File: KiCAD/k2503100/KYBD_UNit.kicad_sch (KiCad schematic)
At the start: 88 parts, among them Q301 2N3904, Q302 2N3904, Q303 2N3904, Q304 2N3904, Q305 2N3904, Q306 2N3904, Q307 2N3904, Q308 2N3904, Q309 2N3904, Q310 2N3904, Q311 2N3904, Q312 2N3904

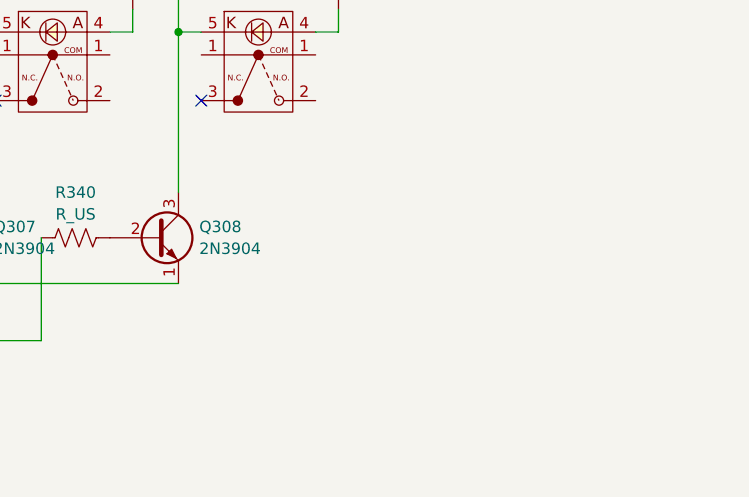
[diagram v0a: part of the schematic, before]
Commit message: 未使用回路の削除
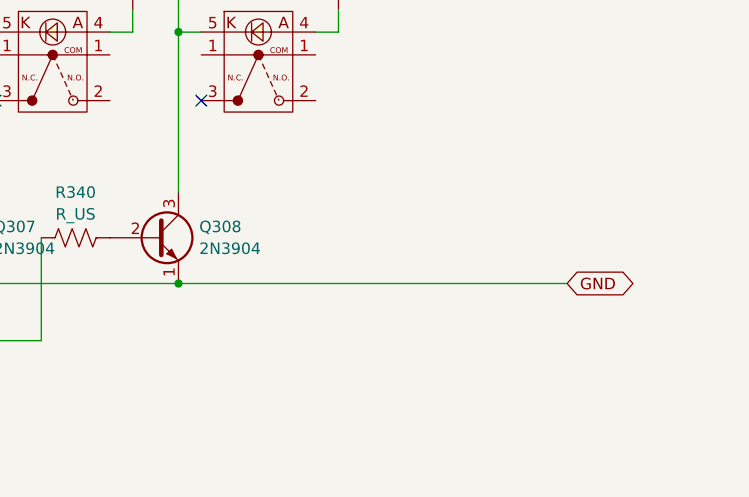
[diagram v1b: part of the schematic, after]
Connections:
- net GND: now reaches Q301.1 (E), Q302.1 (E), Q303.1 (E), Q304.1 (E), Q305.1 (E), Q306.1 (E), Q307.1 (E), Q308.1 (E)
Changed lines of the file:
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@@
 	)
 	(junction
+		(at 213.36 154.94)
+		(diameter 0)
+		(color 0 0 0 0)
+	)
+	(junction
 		(at 231.14 90.17)
 		(diameter 0)
@@
 	(wire
 		(pts
+			(xy 213.36 154.94) (xy 256.54 154.94)
+		)
+		(stroke
+			(width 0)
+			(type default)
+		)
+	)
+	(wire
+		(pts
 			(xy 78.74 127) (xy 76.2 127)
 		)
@@
 		)
 	)
+	(global_label "GND"
+		(shape bidirectional)
+		(at 256.54 154.94 0)
+		(fields_autoplaced yes)
+		(effects
+			(font
+				(size 1.27 1.27)
+			)
+			(justify left)
+		)
+		(property "Intersheetrefs" "${INTERSHEET_REFS}"
+			(at 264.5068 154.94 0)
+			(effects
+				(font
+					(size 1.27 1.27)
+				)
+				(justify left)
+				(hide yes)
+			)
+		)
+	)
 	(global_label "5V"
 		(shape input)
@@
 	)
 	(symbol
-		(lib_name "K2503100:MP86A1")
 		(lib_id "K2503100:MP86A1")
 		(at 153.67 43.18 0)
@@
 	)
 	(symbol
-		(lib_name "K2503100:MP86A1")
 		(lib_id "K2503100:MP86A1")
 		(at 130.81 43.18 0)
@@
 	)
 	(symbol
-		(lib_name "K2503100:MP86A1")
 		(lib_id "K2503100:MP86A1")
 		(at 176.53 96.52 0)
@@
 	)
 	(symbol
-		(lib_name "K2503100:MP86A1")
 		(lib_id "K2503100:MP86A1")
 		(at 62.23 69.85 0)
@@
 	)
 	(symbol
-		(lib_name "K2503100:MP86A1")
 		(lib_id "K2503100:MP86A1")
 		(at 62.23 96.52 0)
@@
 	)
 	(symbol
-		(lib_name "K2503100:MP86A1")
 		(lib_id "K2503100:MP86A1")
 		(at 176.53 69.85 0)
@@
 	)
 	(symbol
-		(lib_name "K2503100:MP86A1")
 		(lib_id "K2503100:MP86A1")
 		(at 199.39 43.18 0)
@@
 	)
 	(symbol
-		(lib_name "K2503100:MP86A1")
 		(lib_id "K2503100:MP86A1")
 		(at 62.23 43.18 0)
@@
 	)
 	(symbol
-		(lib_name "K2503100:MP86A1")
 		(lib_id "K2503100:MP86A1")
 		(at 222.25 96.52 0)
@@
 	)
 	(symbol
-		(lib_name "K2503100:MP86A1")
 		(lib_id "K2503100:MP86A1")
 		(at 85.09 96.52 0)
@@
 	)
 	(symbol
-		(lib_name "K2503100:MP86A1")
 		(lib_id "K2503100:MP86A1")
 		(at 199.39 123.19 0)
@@
 	)
 	(symbol
-		(lib_name "K2503100:MP86A1")
 		(lib_id "K2503100:MP86A1")
 		(at 199.39 96.52 0)
@@
 	)
 	(symbol
-		(lib_name "K2503100:MP86A1")
 		(lib_id "K2503100:MP86A1")
 		(at 199.39 69.85 0)
@@
 	)
 	(symbol
-		(lib_name "K2503100:MP86A1")
 		(lib_id "K2503100:MP86A1")
 		(at 107.95 96.52 0)
@@
 	)
 	(symbol
-		(lib_name "K2503100:MP86A1")
 		(lib_id "K2503100:MP86A1")
 		(at 176.53 43.18 0)
@@
 	)
 	(symbol
-		(lib_name "K2503100:MP86A1")
 		(lib_id "K2503100:MP86A1")
 		(at 222.25 123.19 0)
@@
 	)
 	(symbol
-		(lib_name "K2503100:MP86A1")
 		(lib_id "K2503100:MP86A1")
 		(at 85.09 69.85 0)
@@
 	)
 	(symbol
-		(lib_name "K2503100:MP86A1")
 		(lib_id "K2503100:MP86A1")
 		(at 153.67 96.52 0)
@@
 	)
 	(symbol
-		(lib_name "K2503100:MP86A1")
 		(lib_id "K2503100:MP86A1")
 		(at 130.81 123.19 0)
@@
 	)
 	(symbol
-		(lib_name "K2503100:MP86A1")
 		(lib_id "K2503100:MP86A1")
 		(at 153.67 69.85 0)
@@
 	)
 	(symbol
-		(lib_name "K2503100:MP86A1")
 		(lib_id "K2503100:MP86A1")
 		(at 153.67 123.19 0)
@@
 	)
 	(symbol
-		(lib_name "K2503100:MP86A1")
 		(lib_id "K2503100:MP86A1")
 		(at 176.53 123.19 0)
@@
 	)
 	(symbol
-		(lib_name "K2503100:MP86A1")
 		(lib_id "K2503100:MP86A1")
 		(at 130.81 96.52 0)
@@
 	)
 	(symbol
-		(lib_name "K2503100:MP86A1")
 		(lib_id "K2503100:MP86A1")
 		(at 107.95 69.85 0)
@@
 	)
 	(symbol
-		(lib_name "K2503100:MP86A1")
 		(lib_id "K2503100:MP86A1")
 		(at 62.23 123.19 0)
@@
 	)
 	(symbol
-		(lib_name "K2503100:MP86A1")
 		(lib_id "K2503100:MP86A1")
 		(at 222.25 69.85 0)
@@
 	)
 	(symbol
-		(lib_name "K2503100:MP86A1")
 		(lib_id "K2503100:MP86A1")
 		(at 130.81 69.85 0)
@@
 	)
 	(symbol
-		(lib_name "K2503100:MP86A1")
 		(lib_id "K2503100:MP86A1")
 		(at 85.09 43.18 0)
@@
 	)
 	(symbol
-		(lib_name "K2503100:MP86A1")
 		(lib_id "K2503100:MP86A1")
 		(at 107.95 43.18 0)
@@
 	)
 	(symbol
-		(lib_name "K2503100:MP86A1")
 		(lib_id "K2503100:MP86A1")
 		(at 222.25 43.18 0)
@@
 	)
 	(symbol
-		(lib_name "K2503100:MP86A1")
 		(lib_id "K2503100:MP86A1")
 		(at 85.09 123.19 0)
@@
 	)
 	(symbol
-		(lib_name "K2503100:MP86A1")
 		(lib_id "K2503100:MP86A1")
 		(at 107.95 123.19 0)

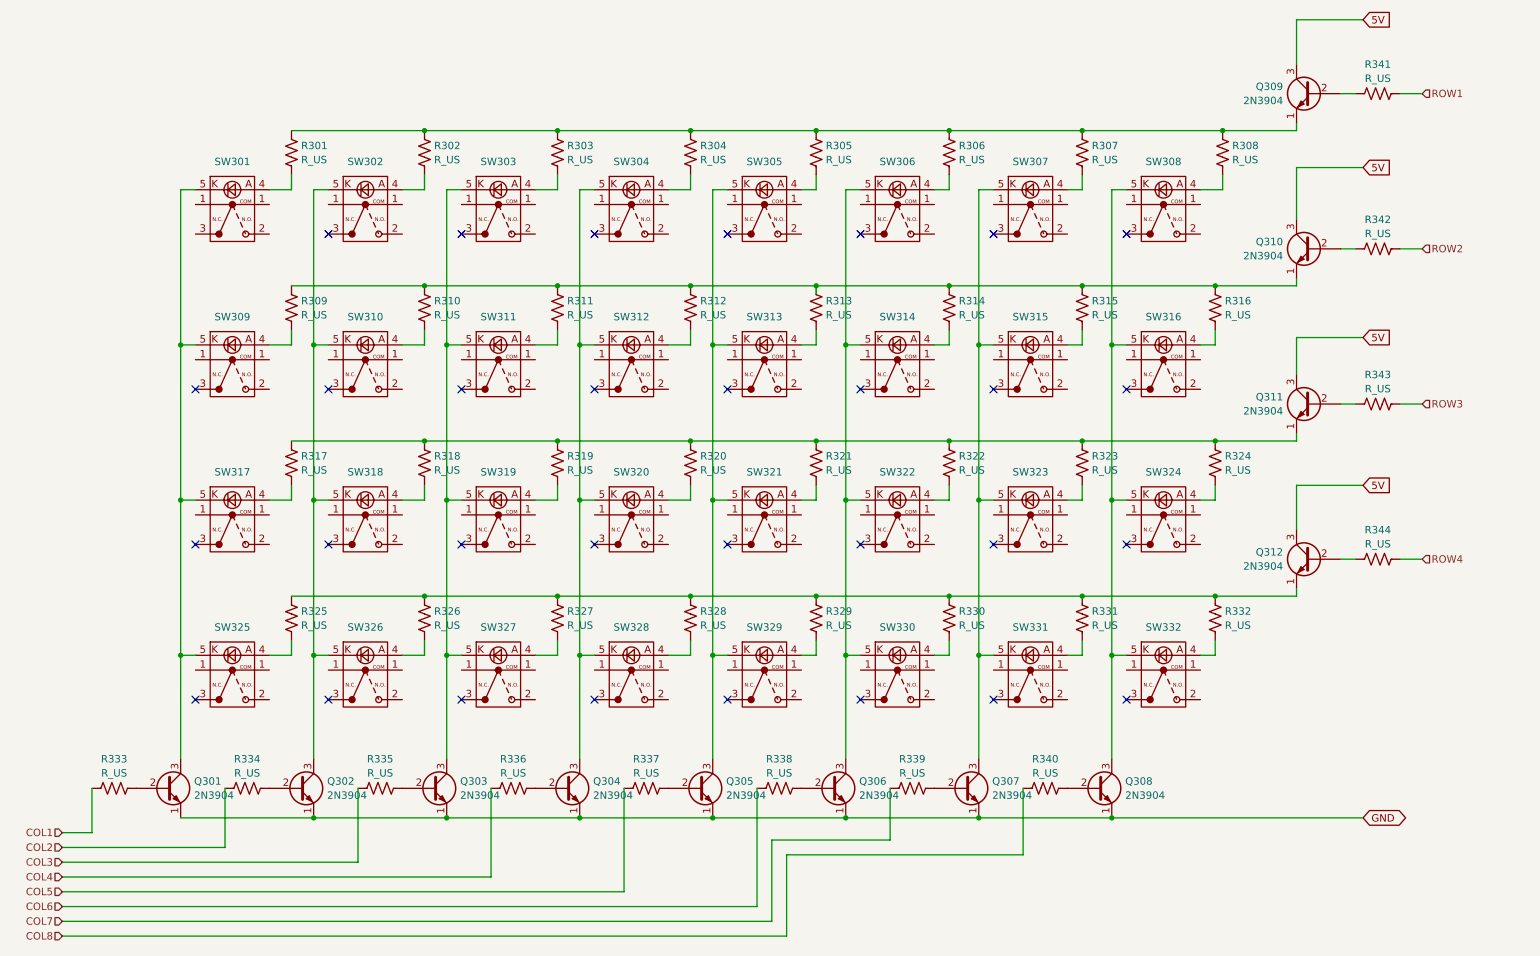
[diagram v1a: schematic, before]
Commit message: KCOL側配線途中
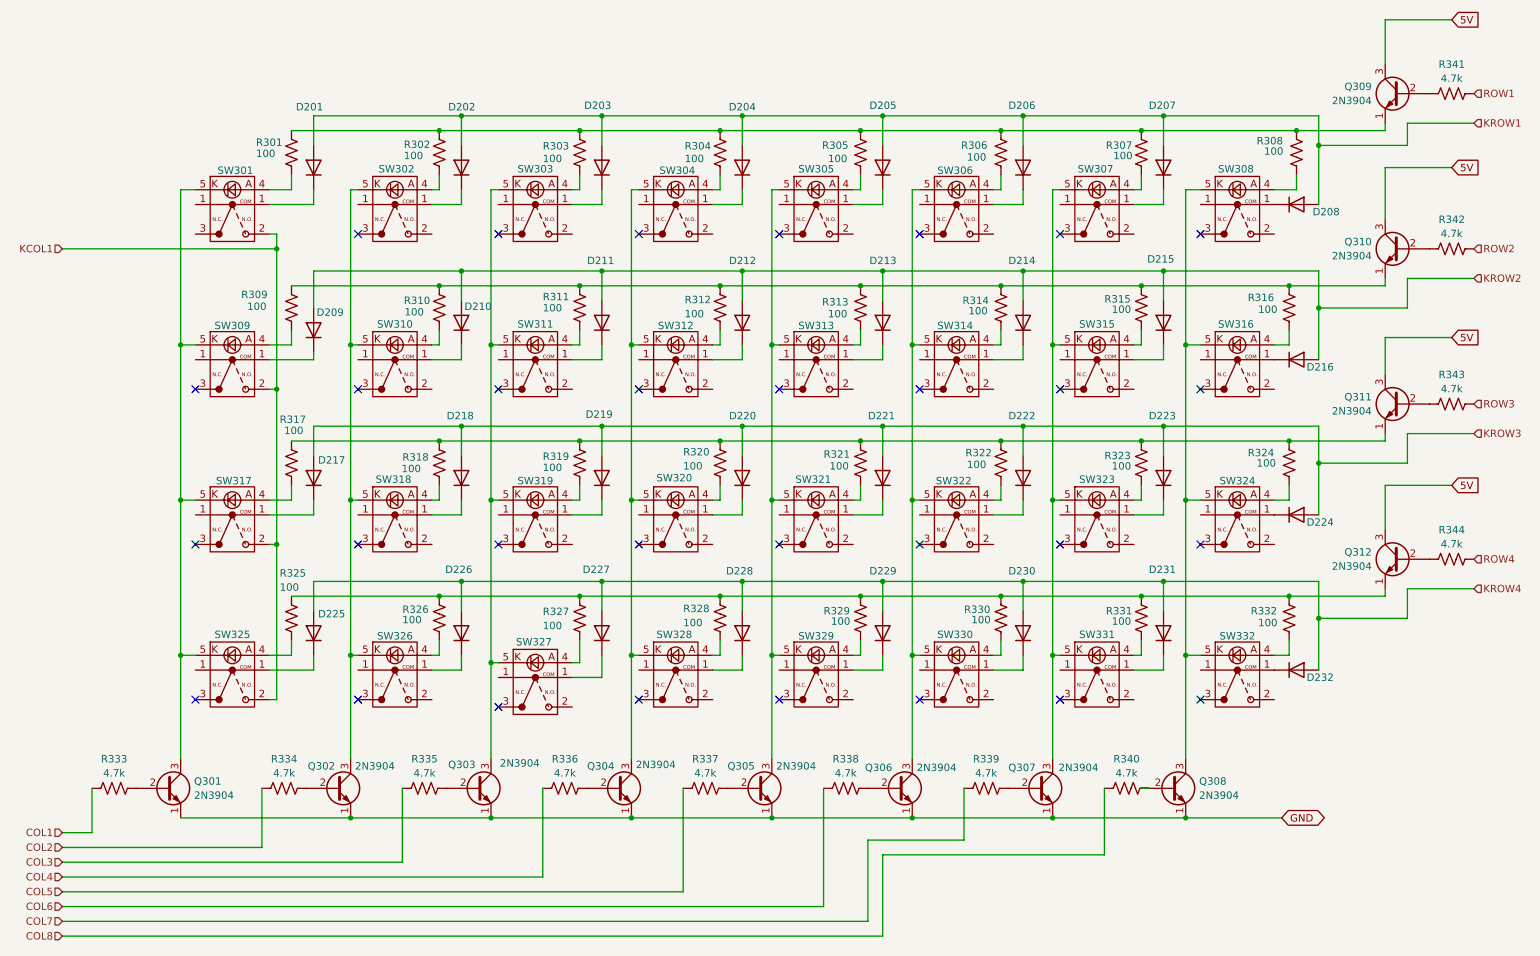
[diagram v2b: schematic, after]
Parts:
- added D201, D202, D203, D204, D205, D206, D207, D208, D209, D210, D211, D212, D213, D214, D215, D216, D217, D218, D219, D220, D221, D222, D223, D224, D225, D226, D227, D228, D229, D230, D231, D232: 1N4148W, Diode_SMD:D_SOD-123, symbol Diode:1N4148W
- R301, R302, R303, R304, R305, R306, R307, R308, R309, R310, R311, R312, R313, R314, R315, R316, R317, R318, R319, R320, R321, R322, R323, R324, R325, R326, R327, R328, R329, R330, R331, R332: value R_US -> 100
- R333, R334, R335, R336, R337, R338, R339, R340, R341, R342, R343, R344: value R_US -> 4.7k
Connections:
- net at SW305.1: now also D205.1 (K)
- net at SW304.1: now also D204.1 (K)
- net at SW322.1: now also D222.1 (K)
- net at SW309.1: now also D209.1 (K)
- net KCOL1: now reaches SW309.2
- net KCOL1: now also SW301.2, SW317.2, SW325.2
- net at SW317.1: now also D217.1 (K)
- net at SW307.1: now also D207.1 (K)
- net at SW301.1: now also D201.1 (K)
- net at SW324.1: now also D224.1 (K)
- net at SW331.1: now also D231.1 (K)
- net at SW323.1: now also D223.1 (K)
- net at SW315.1: now also D215.1 (K)
- net at SW310.1: now also D210.1 (K)
- net at SW313.1: now also D213.1 (K)
- net at SW311.1: now also D211.1 (K)
- new net: D208.1 (K), SW308.1
- new net: D225.1 (K), SW325.1
- new net: D214.1 (K), SW314.1
- new net: D218.1 (K), SW318.1
- new net: D221.1 (K), SW321.1
- new net: D219.1 (K), SW319.1
- new net: D228.1 (K), SW328.1
- new net: D232.1 (K), SW332.1
- new net: D206.1 (K), SW306.1
- new net: D220.1 (K), SW320.1
- new net: D202.1 (K), SW302.1
- new net: D227.1 (K), SW327.1
- new net: D226.1 (K), SW326.1
- new net: D230.1 (K), SW330.1
- new net: D216.1 (K), SW316.1
- new net: D229.1 (K), SW329.1
- new net: D212.1 (K), SW312.1
- new net: D203.1 (K), SW303.1
- new net KROW1: D201.2 (A), D202.2 (A), D203.2 (A), D204.2 (A), D205.2 (A), D206.2 (A), D207.2 (A), D208.2 (A)
- new net KROW2: D209.2 (A), D210.2 (A), D211.2 (A), D212.2 (A), D213.2 (A), D214.2 (A), D215.2 (A), D216.2 (A)
- new net KROW3: D217.2 (A), D218.2 (A), D219.2 (A), D220.2 (A), D221.2 (A), D222.2 (A), D223.2 (A), D224.2 (A)
- new net KROW4: D225.2 (A), D226.2 (A), D227.2 (A), D228.2 (A), D229.2 (A), D230.2 (A), D231.2 (A), D232.2 (A)
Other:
- moved on the sheet: Q302, Q303, Q304, Q305, Q306, Q307, Q308, Q309, Q310, Q311, Q312, R302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

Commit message: KYBD UNIT ほぼ完成
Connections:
- net at SW305.1: now also D205.1 (K)
- net KCOL5: now reaches SW305.2
- net KCOL5: now also SW313.2, SW321.2, SW329.2
- net at SW304.1: now also D204.1 (K)
- net KCOL4: now reaches SW304.2
- net KCOL4: now also SW312.2, SW320.2, SW328.2
- net at SW322.1: now also D222.1 (K)
- net KCOL6: now reaches SW322.2
- net KCOL6: now also SW306.2, SW314.2, SW330.2
- net at SW309.1: now also D209.1 (K)
- net at SW317.1: now also D217.1 (K)
- net at SW307.1: now also D207.1 (K)
- net KCOL7: now reaches SW307.2
- net KCOL7: now also SW315.2, SW323.2, SW331.2
- net at SW301.1: now also D201.1 (K)
- net at SW324.1: now also D224.1 (K)
- net KCOL8: now reaches SW324.2
- net KCOL8: now also SW308.2, SW316.2, SW332.2
- net KCOL2: now reaches SW318.2
- net KCOL2: now also SW302.2, SW310.2, SW326.2
- net at SW331.1: now also D231.1 (K)
- net at SW323.1: now also D223.1 (K)
- net at SW315.1: now also D215.1 (K)
- net KCOL3: now reaches SW319.2
- net KCOL3: now also SW303.2, SW311.2, SW327.2
- net at SW310.1: now also D210.1 (K)
- net at SW313.1: now also D213.1 (K)
- net at SW311.1: now also D211.1 (K)
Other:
- company: (none) -> HOLLY & Co.,Ltd.
- title: (none) -> KYBD UNIT
- moved on the sheet: D210, D211, D212, D213, D214, D215, D216, D218, D219, D220, D221, D222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

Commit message: CPUとの接続途中
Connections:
- net at SW305.1: now also D205.1 (K)
- net at SW304.1: now also D204.1 (K)
- net at SW322.1: now also D222.1 (K)
- net at SW309.1: now also D209.1 (K)
- net at SW317.1: now also D217.1 (K)
- net at SW307.1: now also D207.1 (K)
- net at SW301.1: now also D201.1 (K)
- net at SW324.1: now also D224.1 (K)
- net at SW331.1: now also D231.1 (K)
- net at SW323.1: now also D223.1 (K)
- net at SW315.1: now also D215.1 (K)
- net at SW310.1: now also D210.1 (K)
- net at SW313.1: now also D213.1 (K)
- net at SW311.1: now also D211.1 (K)
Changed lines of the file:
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@@
 	)
 	(symbol
-		(lib_name "K2503100:MP86A1")
 		(lib_id "K2503100:MP86A1")
 		(at 114.3 123.19 0)

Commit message: PDF作成
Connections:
- net at SW305.1: now also D205.1 (K)
- net at SW304.1: now also D204.1 (K)
- net at SW322.1: now also D222.1 (K)
- net at SW309.1: now also D209.1 (K)
- net at SW317.1: now also D217.1 (K)
- net at SW307.1: now also D207.1 (K)
- net at SW301.1: now also D201.1 (K)
- net at SW324.1: now also D224.1 (K)
- net at SW331.1: now also D231.1 (K)
- net at SW323.1: now also D223.1 (K)
- net at SW315.1: now also D215.1 (K)
- net at SW310.1: now also D210.1 (K)
- net at SW313.1: now also D213.1 (K)
- net at SW311.1: now also D211.1 (K)
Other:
- company: HOLLY & Co.,Ltd. -> HOLLY & Co.,Ltd.  Masafumi Horimoto
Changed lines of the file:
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@@
 		(date "2024-08-27")
 		(rev "Rev: 1.00")
-		(company "HOLLY & Co.,Ltd.")
+		(company "HOLLY & Co.,Ltd.  Masafumi Horimoto")
 		(comment 1 "記載のない抵抗は100Ω")
 		(comment 2 "Diode: 1N4148W")

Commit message: 途中
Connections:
- net at SW305.1: now also D205.1 (K)
- net at SW304.1: now also D204.1 (K)
- net at SW322.1: now also D222.1 (K)
- net at SW309.1: now also D209.1 (K)
- net at SW317.1: now also D217.1 (K)
- net at SW307.1: now also D207.1 (K)
- net at SW301.1: now also D201.1 (K)
- net at SW324.1: now also D224.1 (K)
- net at SW331.1: now also D231.1 (K)
- net at SW323.1: now also D223.1 (K)
- net at SW315.1: now also D215.1 (K)
- net at SW310.1: now also D210.1 (K)
- net at SW313.1: now also D213.1 (K)
- net at SW311.1: now also D211.1 (K)
- no-connect marks 31 -> 64
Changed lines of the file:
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@@
 	)
 	(no_connect
+		(at 55.88 129.54)
+	)
+	(no_connect
 		(at 204.47 54.61)
 	)
@@
 	)
 	(no_connect
+		(at 156.21 49.53)
+	)
+	(no_connect
 		(at 107.95 107.95)
 	)
@@
 	)
 	(no_connect
+		(at 83.82 49.53)
+	)
+	(no_connect
 		(at 180.34 134.62)
 	)
 	(no_connect
+		(at 204.47 129.54)
+	)
+	(no_connect
+		(at 204.47 49.53)
+	)
+	(no_connect
+		(at 107.95 49.53)
+	)
+	(no_connect
 		(at 132.08 81.28)
 	)
@@
 	)
 	(no_connect
+		(at 132.08 102.87)
+	)
+	(no_connect
 		(at 204.47 107.95)
 	)
@@
 	)
 	(no_connect
+		(at 132.08 49.53)
+	)
+	(no_connect
+		(at 156.21 76.2)
+	)
+	(no_connect
+		(at 228.6 129.54)
+	)
+	(no_connect
 		(at 132.08 134.62)
 	)
 	(no_connect
+		(at 204.47 102.87)
+	)
+	(no_connect
 		(at 55.88 107.95)
 	)
 	(no_connect
+		(at 83.82 129.54)
+	)
+	(no_connect
 		(at 55.88 134.62)
 	)
@@
 	)
 	(no_connect
+		(at 107.95 102.87)
+	)
+	(no_connect
+		(at 156.21 129.54)
+	)
+	(no_connect
+		(at 228.6 49.53)
+	)
+	(no_connect
+		(at 156.21 102.87)
+	)
+	(no_connect
 		(at 180.34 54.61)
 	)
@@
 	)
 	(no_connect
+		(at 132.08 76.2)
+	)
+	(no_connect
 		(at 180.34 81.28)
 	)
@@
 	)
 	(no_connect
+		(at 228.6 102.87)
+	)
+	(no_connect
+		(at 55.88 102.87)
+	)
+	(no_connect
+		(at 132.08 129.54)
+	)
+	(no_connect
 		(at 156.21 54.61)
 	)
 	(no_connect
+		(at 55.88 76.2)
+	)
+	(no_connect
 		(at 107.95 134.62)
 	)
 	(no_connect
+		(at 180.34 129.54)
+	)
+	(no_connect
+		(at 107.95 129.54)
+	)
+	(no_connect
+		(at 83.82 102.87)
+	)
+	(no_connect
+		(at 107.95 76.2)
+	)
+	(no_connect
 		(at 180.34 107.95)
 	)
 	(no_connect
+		(at 228.6 76.2)
+	)
+	(no_connect
+		(at 180.34 102.87)
+	)
+	(no_connect
 		(at 83.82 134.62)
 	)
 	(no_connect
+		(at 180.34 76.2)
+	)
+	(no_connect
+		(at 83.82 76.2)
+	)
+	(no_connect
+		(at 55.88 49.53)
+	)
+	(no_connect
+		(at 204.47 76.2)
+	)
+	(no_connect
+		(at 55.88 54.61)
+	)
+	(no_connect
 		(at 204.47 81.28)
 	)
@@
 	)
 	(no_connect
+		(at 180.34 49.53)
+	)
+	(no_connect
 		(at 132.08 107.95)
 	)
@@
 		(shape input)
 		(at 33.02 69.85 180)
-		(fields_autoplaced yes)
 		(effects
 			(font
@@
 		(shape input)
 		(at 33.02 74.93 180)
-		(fields_autoplaced yes)
 		(effects
 			(font
@@
 		(shape input)
 		(at 33.02 175.26 180)
-		(fields_autoplaced yes)
 		(effects
 			(font
@@
 		(shape input)
 		(at 275.59 62.23 0)
-		(fields_autoplaced yes)
 		(effects
 			(font
@@
 		(shape input)
 		(at 275.59 115.57 0)
-		(fields_autoplaced yes)
 		(effects
 			(font
@@
 		(shape input)
 		(at 275.59 110.49 0)
-		(fields_autoplaced yes)
 		(effects
 			(font
@@
 		(shape input)
 		(at 33.02 167.64 180)
-		(fields_autoplaced yes)
 		(effects
 			(font
@@
 		(shape input)
 		(at 33.02 160.02 180)
-		(fields_autoplaced yes)
 		(effects
 			(font
@@
 		(shape input)
 		(at 33.02 57.15 180)
-		(fields_autoplaced yes)
 		(effects
 			(font
@@
 		(shape input)
 		(at 33.02 162.56 180)
-		(fields_autoplaced yes)
 		(effects
 			(font
@@
 		(shape input)
 		(at 33.02 165.1 180)
-		(fields_autoplaced yes)
 		(effects
 			(font
@@
 		(shape input)
 		(at 275.59 35.56 0)
-		(fields_autoplaced yes)
 		(effects
 			(font
@@
 		(shape input)
 		(at 33.02 67.31 180)
-		(fields_autoplaced yes)
 		(effects
 			(font
@@
 		(shape input)
 		(at 275.59 57.15 0)
-		(fields_autoplaced yes)
 		(effects
 			(font
@@
 		(shape input)
 		(at 33.02 172.72 180)
-		(fields_autoplaced yes)
 		(effects
 			(font
@@
 		(shape input)
 		(at 33.02 157.48 180)
-		(fields_autoplaced yes)
 		(effects
 			(font
@@
 		(shape input)
 		(at 33.02 64.77 180)
-		(fields_autoplaced yes)
 		(effects
 			(font
@@
 		(shape input)
 		(at 33.02 170.18 180)
-		(fields_autoplaced yes)
 		(effects
 			(font
@@
 		(shape input)
 		(at 275.59 83.82 0)
-		(fields_autoplaced yes)
 		(effects
 			(font
@@
 		(shape input)
 		(at 33.02 72.39 180)
-		(fields_autoplaced yes)
 		(effects
 			(font
@@
 		(shape input)
 		(at 275.59 30.48 0)
-		(fields_autoplaced yes)
 		(effects
 			(font
@@
 		(shape input)
 		(at 275.59 88.9 0)
-		(fields_autoplaced yes)
 		(effects
 			(font
@@
 		(shape input)
 		(at 33.02 62.23 180)
-		(fields_autoplaced yes)
 		(effects
 			(font
@@
 		(shape input)
 		(at 33.02 59.69 180)
-		(fields_autoplaced yes)
 		(effects
 			(font

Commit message: PCBデザイン開始
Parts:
- Q301, Q302, Q303, Q304, Q305, Q306, Q307, Q308, Q309, Q310, Q311, Q312: value 2N3904 -> NNBT3904; footprint Package_TO_SOT_THT:TO-92_Inline -> Package_TO_SOT_SMD:SOT-23_Handsoldering
- R301, R302, R303, R304, R305, R306, R307, R308, R309, R310, R311, R312, R313, R314, R315, R316, R317, R318, R319, R320, R321, R322, R323, R324, R325, R326, R327, R328, R329, R330, R331, R332, R333, R334, R335, R336, R337, R338, R339, R340, R341, R342, R343, R344: footprint (none) -> Resistor_SMD:R_0603_1608Metric_Pad0.98x0.95mm_HandSolder
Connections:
- net at SW305.1: now also D205.1 (K)
- net at SW304.1: now also D204.1 (K)
- net at SW322.1: now also D222.1 (K)
- net at SW309.1: now also D209.1 (K)
- net at SW317.1: now also D217.1 (K)
- net at SW307.1: now also D207.1 (K)
- net at SW301.1: now also D201.1 (K)
- net at SW324.1: now also D224.1 (K)
- net at SW331.1: now also D231.1 (K)
- net at SW323.1: now also D223.1 (K)
- net at SW315.1: now also D215.1 (K)
- net at SW310.1: now also D210.1 (K)
- net at SW313.1: now also D213.1 (K)
- net at SW311.1: now also D211.1 (K)
